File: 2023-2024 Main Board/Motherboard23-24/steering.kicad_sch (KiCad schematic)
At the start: 2 parts, among them J1 Conn_01x06_Pin, U1 ARDUINO_PRO_MINI

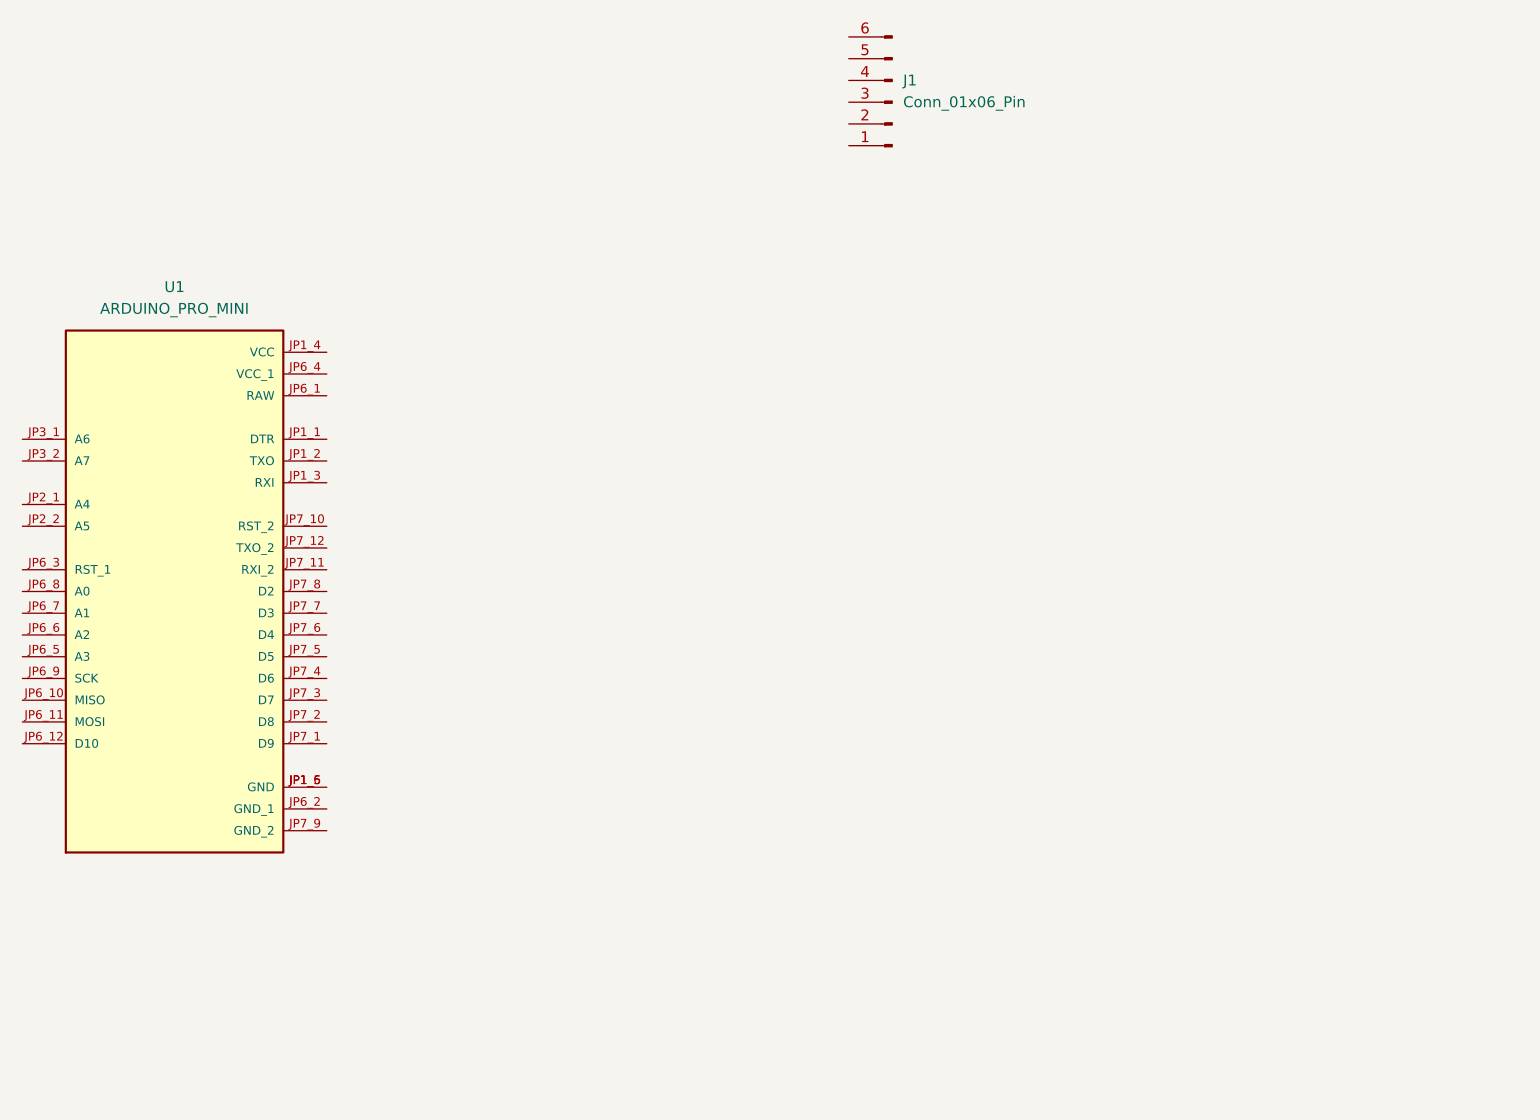
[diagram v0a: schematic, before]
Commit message: Added Schematic for Steering and Throttle
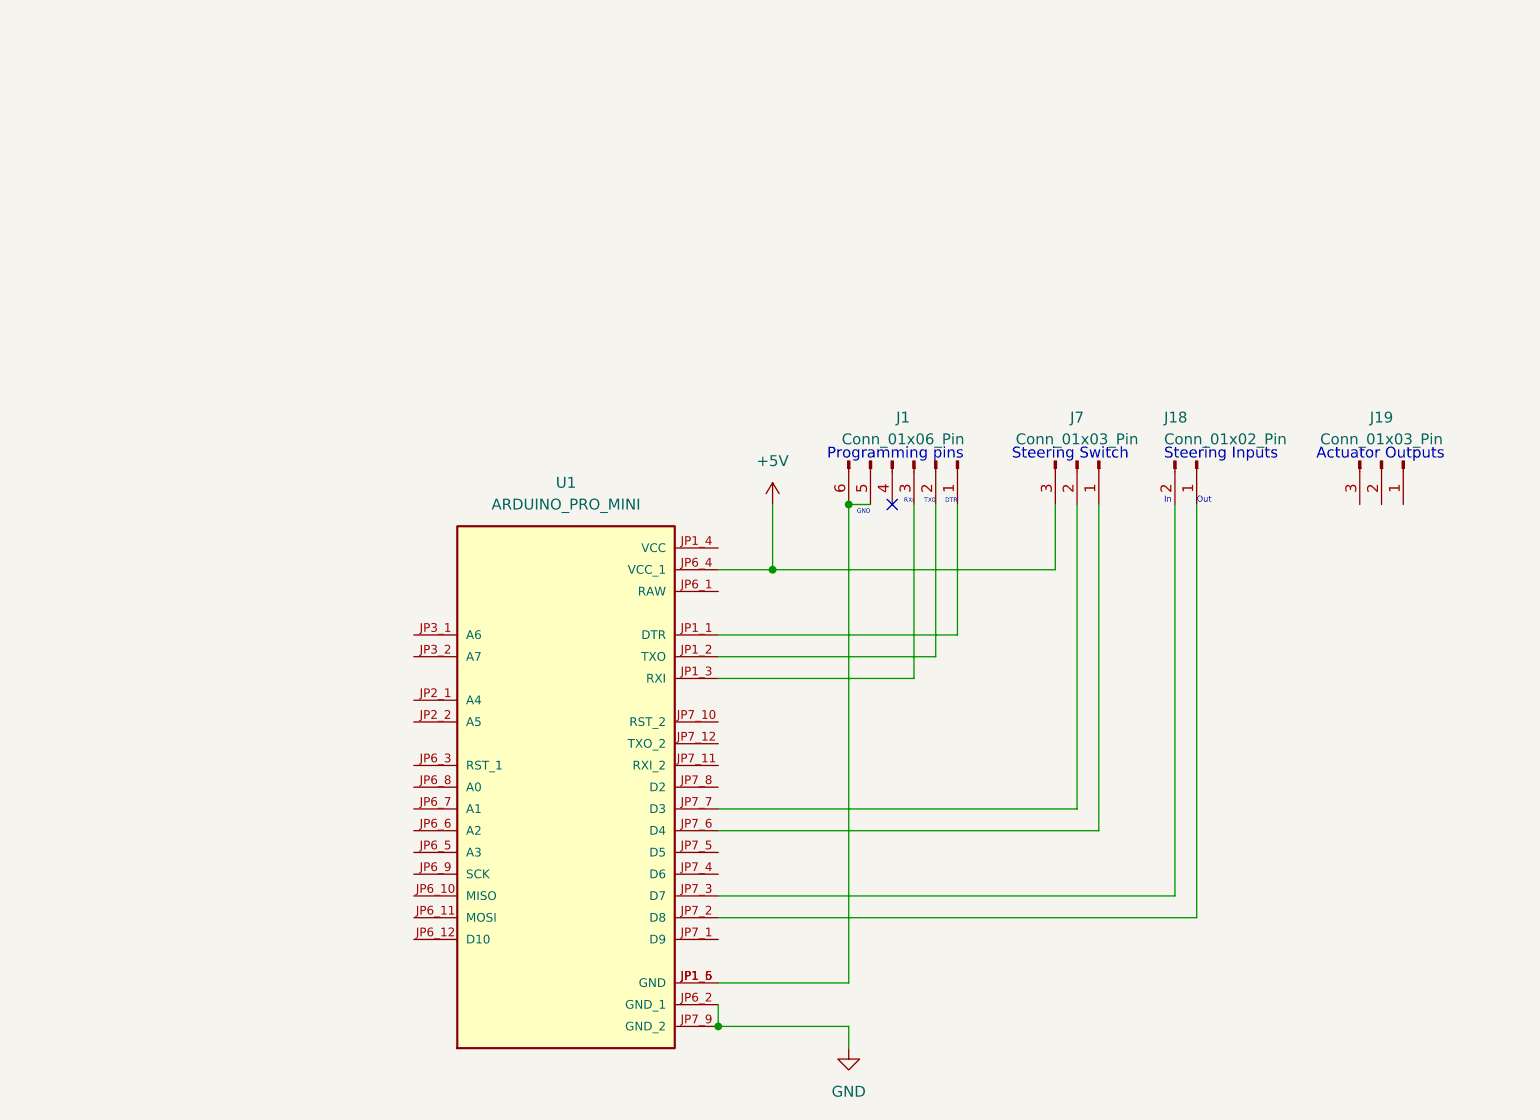
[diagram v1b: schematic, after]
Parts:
- added J18: Conn_01x02_Pin, symbol Connector:Conn_01x02_Pin
- added J19, J7: Conn_01x03_Pin, symbol Connector:Conn_01x03_Pin
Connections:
- net at J1.1 (Pin_1): now also U1.JP1_1 (DTR)
- net at J1.2 (Pin_2): now also U1.JP1_2 (TXO)
- net at J1.3 (Pin_3): now also U1.JP1_3 (RXI)
- net at J1.5 (Pin_5): now also J1.6 (Pin_6), U1.JP1_5 (GND), U1.JP1_6 (GND)
- net GND: now reaches U1.JP6_2 (GND_1)
- net GND: now also U1.JP7_9 (GND_2)
- net +5V: now reaches U1.JP6_4 (VCC_1)
- net +5V: now also J7.3 (Pin_3)
- net at U1.JP7_2 (D8): now also J18.1 (Pin_1)
- net at U1.JP7_3 (D7): now also J18.2 (Pin_2)
- net at U1.JP7_6 (D4): now also J7.1 (Pin_1)
- net at U1.JP7_7 (D3): now also J7.2 (Pin_2)
- no-connect marks 0 -> 1
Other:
- note added: "Actuator Outputs"
- note added: "DTR"
- note added: "GND"
- note added: "In"
- note added: "Out"
- note added: "Programming pins"
- note added: "RXI"
- note added: "Steering Inputs"
- note added: "Steering Switch"
- note added: "TX0"
- moved on the sheet: J1, U1

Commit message: Close to finishing up 2023-2024 Main Board Schematic
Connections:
- net at J7.1 (Pin_1): now also U1.JP7_7 (D3); no longer U1.JP7_6 (D4)
- net at J7.2 (Pin_2): now also U1.JP7_8 (D2); no longer U1.JP7_7 (D3)
- net at J18.1 (Pin_1): now also U1.JP7_5 (D5); no longer U1.JP7_2 (D8)
- net at J18.2 (Pin_2): now also U1.JP7_6 (D4); no longer U1.JP7_3 (D7)
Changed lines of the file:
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@@
     (stroke (width 0) (type default))
   )
-  (wire (pts (xy 166.37 78.74) (xy 166.37 127))
+  (wire (pts (xy 166.37 78.74) (xy 166.37 119.38))
     (stroke (width 0) (type default))
   )
@@
     (stroke (width 0) (type default))
   )
-  (wire (pts (xy 166.37 127) (xy 110.49 127))
+  (wire (pts (xy 166.37 119.38) (xy 110.49 119.38))
     (stroke (width 0) (type default))
   )
-  (wire (pts (xy 110.49 114.3) (xy 152.4 114.3))
+  (wire (pts (xy 110.49 111.76) (xy 152.4 111.76))
     (stroke (width 0) (type default))
   )
@@
     (stroke (width 0) (type default))
   )
-  (wire (pts (xy 154.94 78.74) (xy 154.94 116.84))
+  (wire (pts (xy 154.94 78.74) (xy 154.94 114.3))
     (stroke (width 0) (type default))
   )
@@
     (stroke (width 0) (type default))
   )
-  (wire (pts (xy 163.83 78.74) (xy 163.83 124.46))
+  (wire (pts (xy 163.83 78.74) (xy 163.83 116.84))
     (stroke (width 0) (type default))
   )
-  (wire (pts (xy 163.83 124.46) (xy 110.49 124.46))
+  (wire (pts (xy 163.83 116.84) (xy 110.49 116.84))
     (stroke (width 0) (type default))
   )
@@
     (stroke (width 0) (type default))
   )
-  (wire (pts (xy 154.94 116.84) (xy 110.49 116.84))
+  (wire (pts (xy 154.94 114.3) (xy 110.49 114.3))
     (stroke (width 0) (type default))
   )
-  (wire (pts (xy 152.4 114.3) (xy 152.4 78.74))
+  (wire (pts (xy 152.4 111.76) (xy 152.4 78.74))
     (stroke (width 0) (type default))
   )

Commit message: Added BOM
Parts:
- removed J1: Conn_01x06_Pin, symbol Connector:Conn_01x06_Pin
- removed J19: Conn_01x03_Pin, symbol Connector:Conn_01x03_Pin
- added J19: Conn_01x06_Pin, symbol Connector:Conn_01x06_Pin
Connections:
- net at U1.JP6_6 (A2): now also J19.3 (Pin_3)
- net at U1.JP6_7 (A1): now also J19.2 (Pin_2)
- net at U1.JP6_8 (A0): now also J19.1 (Pin_1)
- net at U1.JP7_1 (D9): now also J19.4 (Pin_4)
- net at U1.JP7_2 (D8): now also J19.5 (Pin_5)
- net at U1.JP7_3 (D7): now also J19.6 (Pin_6)
- no-connect marks 1 -> 0
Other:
- note removed: "DTR"
- note removed: "GND"
- note removed: "Programming pins"
- note removed: "RXI"
- note removed: "TX0"
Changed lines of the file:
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@@
   (junction (at 116.84 86.36) (diameter 0) (color 0 0 0 0)
   )
-  (junction (at 125.73 78.74) (diameter 0) (color 0 0 0 0)
-  )
-  (no_connect (at 130.81 78.74))
+  (wire (pts (xy 69.85 59.69) (xy 69.85 114.3))
+    (stroke (width 0) (type default))
+  )
+  (wire (pts (xy 201.93 83.82) (xy 201.93 59.69))
+    (stroke (width 0) (type default))
+  )
   (wire (pts (xy 149.86 86.36) (xy 149.86 78.74))
     (stroke (width 0) (type default))
   )
-  (wire (pts (xy 125.73 78.74) (xy 128.27 78.74))
+  (wire (pts (xy 187.96 78.74) (xy 187.96 129.54))
     (stroke (width 0) (type default))
   )
@@
     (stroke (width 0) (type default))
   )
-  (wire (pts (xy 125.73 78.74) (xy 125.73 134.62))
+  (wire (pts (xy 182.88 78.74) (xy 182.88 124.46))
+    (stroke (width 0) (type default))
+  )
+  (wire (pts (xy 185.42 127) (xy 110.49 127))
     (stroke (width 0) (type default))
   )
@@
     (stroke (width 0) (type default))
   )
+  (wire (pts (xy 199.39 81.28) (xy 199.39 62.23))
+    (stroke (width 0) (type default))
+  )
+  (wire (pts (xy 72.39 111.76) (xy 74.93 111.76))
+    (stroke (width 0) (type default))
+  )
+  (wire (pts (xy 195.58 81.28) (xy 199.39 81.28))
+    (stroke (width 0) (type default))
+  )
   (wire (pts (xy 154.94 78.74) (xy 154.94 114.3))
     (stroke (width 0) (type default))
   )
-  (wire (pts (xy 138.43 78.74) (xy 138.43 93.98))
-    (stroke (width 0) (type default))
-  )
-  (wire (pts (xy 110.49 96.52) (xy 135.89 96.52))
+  (wire (pts (xy 187.96 129.54) (xy 110.49 129.54))
+    (stroke (width 0) (type default))
+  )
+  (wire (pts (xy 67.31 57.15) (xy 204.47 57.15))
+    (stroke (width 0) (type default))
+  )
+  (wire (pts (xy 72.39 62.23) (xy 199.39 62.23))
+    (stroke (width 0) (type default))
+  )
+  (wire (pts (xy 193.04 83.82) (xy 201.93 83.82))
+    (stroke (width 0) (type default))
+  )
+  (wire (pts (xy 67.31 57.15) (xy 67.31 116.84))
     (stroke (width 0) (type default))
   )
@@
     (stroke (width 0) (type default))
   )
+  (wire (pts (xy 69.85 59.69) (xy 201.93 59.69))
+    (stroke (width 0) (type default))
+  )
   (wire (pts (xy 110.49 86.36) (xy 116.84 86.36))
     (stroke (width 0) (type default))
   )
-  (wire (pts (xy 110.49 93.98) (xy 138.43 93.98))
-    (stroke (width 0) (type default))
-  )
-  (wire (pts (xy 133.35 78.74) (xy 133.35 99.06))
+  (wire (pts (xy 67.31 116.84) (xy 74.93 116.84))
+    (stroke (width 0) (type default))
+  )
+  (wire (pts (xy 190.5 86.36) (xy 204.47 86.36))
+    (stroke (width 0) (type default))
+  )
+  (wire (pts (xy 72.39 62.23) (xy 72.39 111.76))
+    (stroke (width 0) (type default))
+  )
+  (wire (pts (xy 204.47 86.36) (xy 204.47 57.15))
     (stroke (width 0) (type default))
   )
@@
     (stroke (width 0) (type default))
   )
+  (wire (pts (xy 193.04 78.74) (xy 193.04 83.82))
+    (stroke (width 0) (type default))
+  )
   (wire (pts (xy 125.73 139.7) (xy 125.73 142.24))
     (stroke (width 0) (type default))
   )
-  (wire (pts (xy 110.49 99.06) (xy 133.35 99.06))
+  (wire (pts (xy 190.5 78.74) (xy 190.5 86.36))
+    (stroke (width 0) (type default))
+  )
+  (wire (pts (xy 69.85 114.3) (xy 74.93 114.3))
     (stroke (width 0) (type default))
   )
@@
     (stroke (width 0) (type default))
   )
-  (wire (pts (xy 135.89 78.74) (xy 135.89 96.52))
-    (stroke (width 0) (type default))
-  )
   (wire (pts (xy 154.94 114.3) (xy 110.49 114.3))
     (stroke (width 0) (type default))
   )
+  (wire (pts (xy 185.42 78.74) (xy 185.42 127))
+    (stroke (width 0) (type default))
+  )
   (wire (pts (xy 152.4 111.76) (xy 152.4 78.74))
     (stroke (width 0) (type default))
   )
-  (text "RXI" (at 133.35 78.74 0)
-    (effects (font (size 0.508 0.508)) (justify right bottom))
+  (wire (pts (xy 195.58 78.74) (xy 195.58 81.28))
+    (stroke (width 0) (type default))
+  )
+  (wire (pts (xy 182.88 124.46) (xy 110.49 124.46))
+    (stroke (width 0) (type default))
   )
   (text "Steering Switch" (at 144.78 73.66 0)
     (effects (font (size 1.27 1.27)) (justify left bottom))
   )
-  (text "DTR" (at 138.43 78.74 0)
-    (effects (font (size 0.508 0.508)) (justify right bottom))
-  )
   (text "Out" (at 166.37 78.74 0)
     (effects (font (size 0.7 0.7)) (justify left bottom))
   )
-  (text "GND" (at 128.27 80.01 0)
-    (effects (font (size 0.508 0.508)) (justify right bottom))
-  )
-  (text "TX0" (at 135.89 78.74 0)
-    (effects (font (size 0.508 0.508)) (justify right bottom))
-  )
   (text "Actuator Outputs" (at 180.34 73.66 0)
     (effects (font (size 1.27 1.27)) (justify left bottom))
@@
     (effects (font (size 1.27 1.27)) (justify left bottom))
   )
-  (text "Programming pins " (at 123.19 73.66 0)
-    (effects (font (size 1.27 1.27)) (justify left bottom))
-  )
   (text "In" (at 162.56 78.74 0)
     (effects (font (size 0.7 0.7)) (justify left bottom))
@@
     )
   )
-  (symbol (lib_id "Connector:Conn_01x06_Pin") (at 133.35 73.66 270) (unit 1)
-    (in_bom yes) (on_board yes) (dnp no) (fields_autoplaced)
-    (property "Reference" "J1" (at 132.08 68.58 90)
-      (effects (font (size 1.27 1.27)))
-    )
-    (property "Value" "Conn_01x06_Pin" (at 132.08 71.12 90)
-      (effects (font (size 1.27 1.27)))
-    )
-    (property "Footprint" "" (at 133.35 73.66 0)
-      (effects (font (size 1.27 1.27)) hide)
-    )
-    (property "Datasheet" "~" (at 133.35 73.66 0)
+  (symbol (lib_id "power:+5V") (at 116.84 78.74 0) (unit 1)
+    (in_bom yes) (on_board yes) (dnp no) (fields_autoplaced)
+    (property "Reference" "#PWR02" (at 116.84 82.55 0)
+      (effects (font (size 1.27 1.27)) hide)
+    )
+    (property "Value" "+5V" (at 116.84 73.66 0)
+      (effects (font (size 1.27 1.27)))
+    )
+    (property "Footprint" "" (at 116.84 78.74 0)
+      (effects (font (size 1.27 1.27)) hide)
+    )
+    (property "Datasheet" "" (at 116.84 78.74 0)
+      (effects (font (size 1.27 1.27)) hide)
+    )
+    (pin "1")
+    (instances
+      (project "Motherboard23-24"
+        (path "/418d1727-08ff-41e8-954f-e6e13e4fb4ca/97542c42-a706-445d-a930-fc308481bbac"
+          (reference "#PWR02") (unit 1)
+        )
+      )
+    )
+  )
+  (symbol (lib_id "Connector:Conn_01x06_Pin") (at 190.5 73.66 270) (unit 1)
+    (in_bom yes) (on_board yes) (dnp no) (fields_autoplaced)
+    (property "Reference" "J19" (at 189.23 68.58 90)
+      (effects (font (size 1.27 1.27)))
+    )
+    (property "Value" "Conn_01x06_Pin" (at 189.23 71.12 90)
+      (effects (font (size 1.27 1.27)))
+    )
+    (property "Footprint" "" (at 190.5 73.66 0)
+      (effects (font (size 1.27 1.27)) hide)
+    )
+    (property "Datasheet" "~" (at 190.5 73.66 0)
       (effects (font (size 1.27 1.27)) hide)
     )
@@
       (project "Motherboard23-24"
         (path "/418d1727-08ff-41e8-954f-e6e13e4fb4ca/97542c42-a706-445d-a930-fc308481bbac"
-          (reference "J1") (unit 1)
+          (reference "J19") (unit 1)
         )
         (path "/418d1727-08ff-41e8-954f-e6e13e4fb4ca/d15f88a3-eb3a-4abd-b913-7ade9bdcdd4a"
           (reference "J8") (unit 1)
-        )
-      )
-    )
-  )
-  (symbol (lib_id "power:+5V") (at 116.84 78.74 0) (unit 1)
-    (in_bom yes) (on_board yes) (dnp no) (fields_autoplaced)
-    (property "Reference" "#PWR02" (at 116.84 82.55 0)
-      (effects (font (size 1.27 1.27)) hide)
-    )
-    (property "Value" "+5V" (at 116.84 73.66 0)
-      (effects (font (size 1.27 1.27)))
-    )
-    (property "Footprint" "" (at 116.84 78.74 0)
-      (effects (font (size 1.27 1.27)) hide)
-    )
-    (property "Datasheet" "" (at 116.84 78.74 0)
-      (effects (font (size 1.27 1.27)) hide)
-    )
-    (pin "1")
-    (instances
-      (project "Motherboard23-24"
-        (path "/418d1727-08ff-41e8-954f-e6e13e4fb4ca/97542c42-a706-445d-a930-fc308481bbac"
-          (reference "#PWR02") (unit 1)
         )
       )
@@
         )
       )
-    )
-  )
-  (symbol (lib_id "Connector:Conn_01x03_Pin") (at 187.96 73.66 270) (unit 1)
-    (in_bom yes) (on_board yes) (dnp no) (fields_autoplaced)
-    (property "Reference" "J19" (at 187.96 68.58 90)
-      (effects (font (size 1.27 1.27)))
-    )
-    (property "Value" "Conn_01x03_Pin" (at 187.96 71.12 90)
-      (effects (font (size 1.27 1.27)))
-    )
-    (property "Footprint" "" (at 187.96 73.66 0)
-      (effects (font (size 1.27 1.27)) hide)
-    )
-    (property "Datasheet" "~" (at 187.96 73.66 0)
-      (effects (font (size 1.27 1.27)) hide)
-    )
-    (pin "1")
-    (pin "2")
-    (pin "3")
-    (instances
-      (project "Motherboard23-24"
-        (path "/418d1727-08ff-41e8-954f-e6e13e4fb4ca/97542c42-a706-445d-a930-fc308481bbac"
-          (reference "J19") (unit 1)
-        )
-      )

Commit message: first draft of 23-24 Main Board
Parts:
- J18: footprint (none) -> TerminalBlock_Phoenix:TerminalBlock_Phoenix_MKDS-1,5-2-5.08_1x02_P5.08mm_Horizontal
- J19: footprint (none) -> TerminalBlock_Phoenix:TerminalBlock_Phoenix_MKDS-1,5-6-5.08_1x06_P5.08mm_Horizontal
- J7: footprint (none) -> TerminalBlock_Phoenix:TerminalBlock_Phoenix_MKDS-3-3-5.08_1x03_P5.08mm_Horizontal
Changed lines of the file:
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@@
-    (stroke (width 0) (type default))
-  )
-  (wire (pts (xy 125.73 134.62) (xy 110.49 134.62))
     (stroke (width 0) (type default))
   )
@@
       (effects (font (size 1.27 1.27)))
     )
-    (property "Footprint" "" (at 152.4 73.66 0)
+    (property "Footprint" "TerminalBlock_Phoenix:TerminalBlock_Phoenix_MKDS-3-3-5.08_1x03_P5.08mm_Horizontal" (at 152.4 73.66 0)
       (effects (font (size 1.27 1.27)) hide)
     )
@@
       (effects (font (size 1.27 1.27)))
     )
-    (property "Footprint" "" (at 190.5 73.66 0)
+    (property "Footprint" "TerminalBlock_Phoenix:TerminalBlock_Phoenix_MKDS-1,5-6-5.08_1x06_P5.08mm_Horizontal" (at 190.5 73.66 0)
       (effects (font (size 1.27 1.27)) hide)
     )
@@
       (effects (font (size 1.27 1.27)) (justify left))
     )
-    (property "Footprint" "" (at 166.37 73.66 0)
-      (effects (font (size 1.27 1.27)) hide)
-    )
+    (property "Footprint" "TerminalBlock_Phoenix:TerminalBlock_Phoenix_MKDS-1,5-2-5.08_1x02_P5.08mm_Horizontal" (at 166.37 73.66 0)
+      (effects (font (size 1.27 1.27)) hide)
+    )
